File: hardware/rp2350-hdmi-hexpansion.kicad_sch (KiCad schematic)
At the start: 6 parts, among them J1 Hexpansion-Connector

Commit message: hardware: schematic v0.1 with JLCPCB parts, BOMs generated from it
- rp2350-hdmi-hexpansion.kicad_sch: full schematic on one A1 sheet
  (RP2354A, TPS2116 mux + TLV62569 buck, TPS61023 HDMI boost, HDMI Type A
  with TPD4E05U06 ESD and PCA9306 DDC, USB-C sink, microSD, Qwiic, SWD,
  DNP PSRAM and EEPROM). Nets via labels; ERC clean except the intended
  HEXP_DET-to-GND warning; netlist checked pin-for-pin against the design.
  Template edge connector, mounting holes and jumper keep their UUIDs.
- lib/jlc.*: symbols, footprints and .wrl 3D models for all 44 LCSC parts
  (easyeda2kicad), added to the project library tables. STEP models are
  git-ignored.
- bom.csv and hexpansion_bom.xlsx regenerated from the schematic with LCSC
  numbers, JLC Basic/Extended, stock and 10-board prices (107 placements,
  about $5.63/board).
- README/HISTORY: design changes, pin-map changes (GPIO27 RGB, 28 badge
  sense, 29 boost EN), backfeed addendum, firmware follow-ups, and open
  items (LS_A/RUN leak, HS_G/HS_H crossing only confirmed on port 4).
  Corrects the PSRAM part: APS6404L-3SQR-ZR is USON-8, the SOP-8 is -SN.

Co-Authored-By: Claude Opus 5.5 <noreply@anthropic.com>
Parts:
- removed D1: LED, LED_SMD:LED_0805_2012Metric, symbol Device:LED
- removed R1: R, Resistor_SMD:R_0603_1608Metric, symbol Device:R
- added C1, C10, C11, C12, C19, C2, C20, C27, C28, C29, C3, C30, C32, C4, C5, C6, C7, C8, C9: 100nF, jlc:C0402, symbol jlc:CL05B104KO5NNNC
- added C13, C14, C15, C31: 4.7uF, jlc:C0402, symbol jlc:CL05A475MP5NRNC
- added C16, C21, C23, C25: 10uF, jlc:C0603, symbol jlc:CL10A106KP8NNNC
- added C17, C18: 15pF, jlc:C0402, symbol jlc:0402CG150J500NT
- added C22, C24, C26: 22uF, jlc:C0805, symbol jlc:CL21A226MAQNNNE
- added D1: SMF5.0A, jlc:SOD-123FL_L2.7-W1.8-LS3.8-RD, symbol jlc:SMF5.0A_C19077497
- added F1: 200mA PTC, jlc:F0805, symbol jlc:JK-SMD0805-020-30V
- added J1: HDMI-A, jlc:HDMI-SMD_19P-P0.50-H-F, symbol jlc:HDMI-001
- added J2: USB-C, jlc:USB-C-SMD_TYPE-C-16PIN-2MD-073, symbol jlc:TYPE-C16PIN2MD
- added J3: SWD, jlc:CONN-SMD-3P-P1.00_BM03B-SRSS-TB-LF-SN, symbol jlc:BM03B-SRSS-TB
- added J4: Qwiic, jlc:CONN-SMD_4P-P1.00_SM04B-SRSS-TB-LF-SN, symbol jlc:SM04B-SRSS-TB
- added J5: microSD, jlc:TF-SMD_TF-01A, symbol jlc:TF-01A
- added L1: 3.3uH, jlc:IND-SMD_L2.0-W1.6_AOTA-B201610S3R3-101-T, symbol jlc:AOTA-B201610S3R3-101-T
- added L2: 2.2uH, jlc:IND-SMD_L2.5-W2.0_MHCHL2520, symbol jlc:FTC252012S2R2MBCA
- added L3: 1uH, jlc:IND-SMD_L2.5-W2.0_FTC252010S, symbol jlc:FTC252010S1R0MBCA
- added LED1: PWR, jlc:LED-SMD_L1.6-W0.8-R-RD, symbol jlc:KT-0603R
- added LED2: STATUS, jlc:LED-SMD_L1.6-W0.8-R-RD, symbol jlc:KT-0603R
- added LED3: SK6805, jlc:LED-SMD_4P-L2.7-W2.4_SK6805MICRO-J, symbol jlc:SK6805MICRO-J
- added R1, R36, R37, R38, R39: 33R, jlc:R0402, symbol jlc:0402WGF330JTCE
- added R10, R11: 27R, jlc:R0402, symbol jlc:0402WGF270JTCE
- added R12, R16, R17, R18, R34, R35: 100k, jlc:R0402, symbol jlc:0402WGF1003TCE
- added R13, R15: 22k, jlc:R0402, symbol jlc:0402WGF2202TCE
- added R14: 33k, jlc:R0402, symbol jlc:0402WGF3302TCE
- added R19, R29: 200k, jlc:R0402, symbol jlc:0402WGF2003TCE
- added R2, R40, R51, R6: 1k, jlc:R0402, symbol jlc:0402WGF1001TCE
- added R20: 27k, jlc:R0402, symbol jlc:0402WGF2702TCE
- added R21, R22, R23, R24, R25, R26, R27, R28, R4: 0R, jlc:R0402, symbol jlc:0402WGF0000TCE
- added R3, R41, R42, R43, R44, R45, R46, R47, R5, R7: 10k, jlc:R0402, symbol jlc:0402WGF1002TCE
- added R30, R31, R48, R49, R50: 4.7k, jlc:R0402, symbol jlc:0402WGF4701TCE
- added R32, R33: 2k, jlc:R0402, symbol jlc:0402WGF2001TCE
- added R52: 330R, jlc:R0402, symbol jlc:0402WGF3300TCE
- added R8, R9: 5.1k, jlc:R0402, symbol jlc:0402WGF5101TCE
- added SW1: BOOTSEL, jlc:SW-SMD_L3.9-W3.0-P4.45, symbol jlc:TS-1088-AR02016
- added SW2: RESET, jlc:SW-SMD_L3.9-W3.0-P4.45, symbol jlc:TS-1088-AR02016
- added TP1: +3V3, TestPoint:TestPoint_Pad_D1.0mm, symbol Connector:TestPoint
- added TP2: V5_HDMI, TestPoint:TestPoint_Pad_D1.0mm, symbol Connector:TestPoint
- added TP3: GND, TestPoint:TestPoint_Pad_D1.0mm, symbol Connector:TestPoint
- added U1: RP2354A, jlc:QFN-60_L7.0-W7.0-P0.40-TL-EP3.4, symbol jlc:RP2354A
- added U10: ZD24C64A (fallback), jlc:SOP-8_L4.9-W3.9-P1.27-LS6.0-BL, symbol jlc:ZD24C64A-SSGMT
- added U2: TPS2116DRLR, jlc:SOT-583-8_L2.1-W1.6-P0.50-LS1.6-BL, symbol jlc:TPS2116DRLR
- added U3: TLV62569DBVR, jlc:SOT-23-5_L3.0-W1.7-P0.95-LS2.8-BR, symbol jlc:TLV62569DBVR
- added U4: TPS61023DRLR, jlc:SOT-563_L1.6-W1.2-P0.50-LS1.6-BR, symbol jlc:TPS61023DRLR
- added U5: PCA9306DCUR, jlc:SSOP-8_L2.0-W2.3-P0.50-LS3.1-BR, symbol jlc:PCA9306DCUR
- added U6, U7: TPD4E05U06, jlc:USON-10_L2.5-W1.0-P0.50-BL, symbol jlc:TPD4E05U06DQAR_C138714
- added U8: USBLC6-2SC6, jlc:SOT-23-6_L2.9-W1.6-P0.95-LS2.8-BL, symbol jlc:USBLC6-2SC6_C2687116
- added U9: APS6404L-3SQR-SN, jlc:SOIC-8_L4.9-W3.9-P1.27-LS6.0-BL, symbol jlc:APS6404L-3SQR-SN_C5333729
- added Y1: 12MHz, jlc:CRYSTAL-SMD_4P-L3.2-W2.5-BL, symbol jlc:ABM8-272-T3_C20625731
- H1, H2: value MountingHole_Pad -> MountingHole
- J6: renamed from J1; now in the parts list
- JP1: value SolderJumper_2_Bridged -> Qwiic pull-ups
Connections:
- net GND: now also J6.6 (HEXP_DET), C1.2, C10.2, C11.2, C12.2, C13.2, C14.2, C15.2, C16.2, C17.2, C18.2, C19.2, C2.2, C20.2, C21.2, C22.2, C23.2, C24.2, C25.2, C26.2, C27.2, C28.2, C29.2, C3.2, C30.2, C31.2, C32.2, C4.2, C5.2, C6.2, C7.2, C8.2, C9.2, D1.2 (A), J1.11 (TMDSClockShield), J1.17 (DDC/CECGround), J1.2 (TMDSData2Shield), J1.20, J1.21, J1.22, J1.23, J1.5 (TMDSData1Shield), J1.8 (TMDSData0Shield), J2.13 (EH), J2.14 (EH), J2.A1B12 (GND), J2.B1A12 (GND), J3.2, J4.1, J5.10 (GND), J5.11 (GND), J5.12 (GND), J5.13 (GND), J5.6 (VSS), LED1.2 (K), LED2.2 (K), LED3.1 (GND), R13.2, R15.2, R17.2, R18.2, R20.2, R35.2, R8.2, R9.2, SW1.2, SW2.2, TP3.1, U1.47 (VREG_PGND), U1.61 (EP), U10.1 (A0), U10.2 (A1), U10.3 (A2), U10.4 (GND), U10.7 (WP), U2.1 (GND), U3.2 (GND), U4.4 (GND), U5.1 (GND), U6.3 (GND), U6.8 (GND), U7.3 (GND), U7.8 (GND), U8.2 (GND), U9.4 (VSS), Y1.2 (GND), Y1.4 (GND); no longer JP1.2 (B)
- net HS_F: now also R36.1
- net HS_G: now also R38.1
- net HS_H: now also R37.1, R41.2
- net HS_I: now also R39.1
- net LS_A: now reaches J6.2 (LS_A)
- net LS_A: now also R4.1
- net LS_B: now reaches J6.3 (LS_B)
- net LS_B: now also R40.1
- net 3V3 renamed 3V3_BADGE
- net 3V3_BADGE: now also C23.1, C29.1, R16.1, R41.1, U10.8 (VCC), U2.6 (VIN2)
- net HEXP_DET renamed +3V3
- net +3V3: now also C1.1, C14.1, C16.1, C2.1, C20.1, C24.1, C25.1, C3.1, C30.1, C31.1, C32.1, C4.1, C5.1, C6.1, C7.1, C8.1, C9.1, J4.2, J5.4 (VDD), L3.1, LED3.3 (VDD), R1.1, R3.1, R30.1, R31.1, R42.1, R43.1, R44.1, R45.1, R46.1, R47.1, R5.1, R50.1, R7.1, TP1.1, U1.1 (IOVDD), U1.11 (IOVDD), U1.20 (IOVDD), U1.30 (IOVDD), U1.38 (IOVDD), U1.44 (ADC_AVDD), U1.45 (IOVDD), U1.49 (VREG_VIN), U1.53 (USB_OTP_VDD), U1.54 (QSPI_IOVDD), U2.2 (VOUT), U2.7 (VOUT), U4.3 (VIN), U5.2 (VREF1), U9.8 (VDD); no longer J6.6 (HEXP_DET)
- net LS_C: no longer names the net of J6.7 (LS_C)
- net LS_D: no longer names the net of J6.8 (LS_D)
- net LS_E: no longer names the net of J6.9 (LS_E)
- net SCL renamed BADGE_SCL
- net BADGE_SCL: now also U1.37 (GPIO25), U10.6 (SCL)
- net SDA renamed BADGE_SDA
- net BADGE_SDA: now also U1.36 (GPIO24), U10.5 (SDA)
- new net 3V3_USB: C22.1, L2.2, R12.1, R14.1, U2.3 (VIN1), U2.5 (MODE)
- new net BADGE_IRQ: R40.2, U1.40 (GPIO26_ADC0)
- new net BADGE_SENSE: R16.2, R17.1, U1.42 (GPIO28_ADC2)
- new net BOOST_EN: R18.1, U1.43 (GPIO29_ADC3), U4.2 (EN)
- new net BOOST_FB: R19.2, R20.1, U4.1 (FB)
- new net BOOST_SW: L3.2, U4.5 (SW)
- new net BOOTSEL_SW: R6.2, SW1.1
- new net BUCK_FB: R12.2, R13.1, U3.5 (FB)
- new net BUCK_SW: L2.1, U3.3 (SW)
- new net CC1: J2.A5 (CC1), R8.1
- new net CC2: J2.B5 (CC2), R9.1
- new net DDC_EN: C28.1, R29.2, U5.7 (VREF2), U5.8 (EN)
- new net DDC_SCL_3V3: R30.2, U1.7 (GPIO4), U5.3 (SCL1)
- new net DDC_SDA_3V3: R31.2, U1.5 (GPIO3), U5.4 (SDA1)
- new net DVDD: C10.1, C11.1, C12.1, C13.1, L1.2, U1.23 (DVDD), U1.39 (DVDD), U1.50 (VREG_FB), U1.6 (DVDD)
- new net HDMI_CK_N: J1.12 (TMDSClock-), R24.2, U6.5 (D2-), U6.6 (NC)
- new net HDMI_CK_P: J1.10 (TMDSClock+), R23.2, U6.4 (D2+), U6.7 (NC)
- new net HDMI_D0_N: J1.9 (TMDSData0-), R28.2, U7.5 (D2-), U7.6 (NC)
- new net HDMI_D0_P: J1.7 (TMDSData0+), R27.2, U7.4 (D2+), U7.7 (NC)
- new net HDMI_D1_N: J1.6 (TMDSData1-), R26.2, U7.2 (D1-), U7.9 (NC)
- new net HDMI_D1_P: J1.4 (TMDSData1+), R25.2, U7.1 (D1+), U7.10 (NC)
- new net HDMI_D2_N: J1.3 (TMDSData2-), R22.2, U6.2 (D1-), U6.9 (NC)
- new net HDMI_D2_P: J1.1 (TMDSData2+), R21.2, U6.1 (D1+), U6.10 (NC)
- new net HDMI_HPD: J1.19 (HotPlugDetect), R34.1
- new net HDMI_SCL: J1.15 (SCL), R32.2, U5.6 (SCL2)
- new net HDMI_SDA: J1.16 (SDA), R33.2, U5.5 (SDA2)
- new net HPD_SENSE: R34.2, R35.1, U1.4 (GPIO2)
- new net LED1_A: LED1.1 (A), R50.2
- new net LED2_A: LED2.1 (A), R51.2
- new net LED_STATUS: R51.1, U1.3 (GPIO1)
- new net MUX_PR1: R14.2, R15.1, U2.4 (PR1)
- new net PSRAM_CS: R7.2, U1.2 (GPIO0), U9.1 (~{CE})
- new net QSPI_SCLK: U1.56 (QSPI_SCLK), U9.6 (SCLK)
- new net QSPI_SD0: U1.57 (QSPI_SD0), U9.5 (SI/SIO[0])
- new net QSPI_SD1: U1.59 (QSPI_SD1), U9.2 (SO/SIO[1])
- new net QSPI_SD2: U1.58 (QSPI_SD2), U9.3 (SIO[2])
- new net QSPI_SD3: U1.55 (QSPI_SD3), U9.7 (SIO[3])
- new net QSPI_SS: R5.2, R6.1, U1.60 (QSPI_SS)
- new net QWIIC_PU: JP1.2 (B), R48.1, R49.1
- new net QWIIC_SCL: J4.4, R49.2, U1.10 (GPIO7)
- new net QWIIC_SDA: J4.3, R48.2, U1.9 (GPIO6)
- new net RGB_DIN: R52.1, U1.41 (GPIO27_ADC1)
- new net RGB_DIN_R: LED3.2 (DIN), R52.2
- new net RUN: C19.1, R3.2, R4.2, SW2.1, U1.26 (RUN)
- new net SD_CD: J5.9 (CD), R47.2, U1.8 (GPIO5)
- new net SD_CS: J5.2 (CDDAT3(CS)), R43.2, U1.13 (GPIO9)
- new net SD_DAT1: J5.8 (DAT1(RSV)), R46.2
- new net SD_DAT2: J5.1 (DAT2(RSV)), R42.2
- new net SD_MISO: J5.7 (DAT0(D0)), R45.2, U1.12 (GPIO8)
- new net SD_MOSI: J5.3 (CMD(DI)), R44.2, U1.15 (GPIO11)
- new net SD_SCK: J5.5 (CLK(SCLK)), U1.14 (GPIO10)
- new net SPI_CS: R37.2, U1.33 (GPIO21)
- new net SPI_MISO: R39.2, U1.35 (GPIO23)
- new net SPI_MOSI: R36.2, U1.32 (GPIO20)
- new net SPI_SCK: R38.2, U1.34 (GPIO22)
- new net SWCLK: J3.1, U1.24 (SWCLK)
- new net SWDIO: J3.3, U1.25 (SWDIO)
- new net TMDS_CK_N: R24.1, U1.19 (GPIO15)
- new net TMDS_CK_P: R23.1, U1.18 (GPIO14)
- new net TMDS_D0_N: R28.1, U1.31 (GPIO19)
- new net TMDS_D0_P: R27.1, U1.29 (GPIO18)
- new net TMDS_D1_N: R26.1, U1.28 (GPIO17)
- new net TMDS_D1_P: R25.1, U1.27 (GPIO16)
- new net TMDS_D2_N: R22.1, U1.17 (GPIO13)
- new net TMDS_D2_P: R21.1, U1.16 (GPIO12)
- new net USB_CONN_DN: J2.A7 (Dn1), J2.B7 (Dn2), R11.1, U8.3 (I/O2), U8.4 (I/O2)
- new net USB_CONN_DP: J2.A6 (Dp1), J2.B6 (Dp2), R10.1, U8.1 (I/O1), U8.6 (I/O1)
- new net USB_DN: R11.2, U1.51 (USB_DM)
- new net USB_DP: R10.2, U1.52 (USB_DP)
- new net V5_BOOST: C26.1, F1.1, R19.1, U4.6 (VOUT)
- new net V5_HDMI: C27.1, F1.2, J1.18 (+5VPower), R29.1, R32.1, R33.1, TP2.1
- new net VBUS: C21.1, D1.1 (K), J2.A4B9 (VBUS), J2.B4A9 (VBUS), U3.1 (EN), U3.4 (VIN), U8.5 (VBUS)
- new net VREG_AVDD: C15.1, R1.2, U1.46 (VREG_AVDD)
- new net VREG_LX: L1.1, U1.48 (VREG_LX)
- new net XIN: C17.1, U1.21 (XIN), Y1.1
- new net XOUT: R2.1, U1.22 (XOUT)
- new net XOUT_XTAL: C18.1, R2.2, Y1.3
- no-connect marks 0 -> 13
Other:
- note added: "HDMI +5V boost (enabled by GPIO29)"
- note added: "HDMI Type A (DVI over HSTX)"
- note added: "Hexpansion edge connector (badge side)"
- note added: "LEDs, test pads, mounting"
- note added: "MCU - RP2354A (2 MB flash in package)"
- note added: "Notes: - Design rule: this hexpansion never powers the badge (HISTORY.md section 4.5). - Pull-ups on badge-facing lines go to 3V3_BADGE, never +3V3. No pull-ups on BADGE_SDA/SCL (badge has them). - Firmware: tri-state SPI_MISO and BADGE_IRQ until BADGE_SENSE (GPIO28) reads the badge rail live. - Firmware: do not enable internal pull-ups on BADGE_SDA/SCL (GPIO24/25). - OPEN: RUN pull-up (R3) can l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"
- note added: "PSRAM - DNP, hand-solder (QSPI CS1 = GPIO0)"
- note added: "Power mux - never back-powers the badge"
- note added: "Reset, BOOTSEL, SWD"
- note added: "USB-C input (sink only) and 5V -> 3V3 buck"
- note added: "microSD (SPI1) and Qwiic (I2C1)"
- title: (none) -> Hexi-GFX RP2354A HDMI hexpansion
- moved on the sheet: J6

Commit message: hardware: trim schematic - drop DDC, microSD, 0R TMDS and extra passives
- Drop HDMI DDC/EDID (U5 PCA9306 + 6 passives): output is fixed
  640x480@60, so nothing to read. HPD kept on GPIO2.
- Drop microSD (J5, 2 pull-ups, 1 cap): frees the second side flat.
- Drop the eight 0R TMDS insurance resistors; GPIO12-19 drive the ESD
  arrays and socket directly, as on the bench.
- Decoupling cut to the Raspberry Pi minimal design (7 x 100nF on 3V3,
  pins 44/45 and 53/54 share); no BOOTSEL pull-up (internal), no RUN
  debounce cap, no extra HDMI 5V / SD caps.
- Spare GPIOs now 3, 4, 5, 8-11 (no-connect).
- ERC clean except the intended HEXP_DET warning; netlist re-verified
  pin-for-pin (337 pins).
- BOMs regenerated: 78 JLC placements, about $5.01/board (was 107, $5.63).
- README/HISTORY updated with the trims and the microSD decision.

Co-Authored-By: Claude Opus 5.5 <noreply@anthropic.com>
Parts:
- removed C19, C27, C28, C30, C8, C9: 100nF, jlc:C0402, symbol jlc:CL05B104KO5NNNC
- removed C31: 4.7uF, jlc:C0402, symbol jlc:CL05A475MP5NRNC
- removed J5: microSD, jlc:TF-SMD_TF-01A, symbol jlc:TF-01A
- removed R21, R22, R23, R24, R25, R26, R27, R28: 0R, jlc:R0402, symbol jlc:0402WGF0000TCE
- removed R29: 200k, jlc:R0402, symbol jlc:0402WGF2003TCE
- removed R30, R31: 4.7k, jlc:R0402, symbol jlc:0402WGF4701TCE
- removed R32, R33: 2k, jlc:R0402, symbol jlc:0402WGF2001TCE
- removed R42, R43, R44, R45, R46, R47, R5: 10k, jlc:R0402, symbol jlc:0402WGF1002TCE
- removed U5: PCA9306DCUR, jlc:SSOP-8_L2.0-W2.3-P0.50-LS3.1-BR, symbol jlc:PCA9306DCUR
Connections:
- net TMDS_CK_N is gone; now on net HDMI_CK_N: U1.19 (GPIO15)
- net TMDS_CK_P is gone; now on net HDMI_CK_P: U1.18 (GPIO14)
- net TMDS_D0_N is gone; now on net HDMI_D0_N: U1.31 (GPIO19)
- net TMDS_D0_P is gone; now on net HDMI_D0_P: U1.29 (GPIO18)
- net TMDS_D1_N is gone; now on net HDMI_D1_N: U1.28 (GPIO17)
- net TMDS_D1_P is gone; now on net HDMI_D1_P: U1.27 (GPIO16)
- net TMDS_D2_N is gone; now on net HDMI_D2_N: U1.17 (GPIO13)
- net TMDS_D2_P is gone; now on net HDMI_D2_P: U1.16 (GPIO12)
- net DDC_SCL_3V3: no longer names the net of U1.7 (GPIO4)
- net DDC_SDA_3V3: no longer names the net of U1.5 (GPIO3)
- net HDMI_SCL: no longer names the net of J1.15 (SCL)
- net HDMI_SDA: no longer names the net of J1.16 (SDA)
- net SD_CD: no longer names the net of U1.8 (GPIO5)
- net SD_CS: no longer names the net of U1.13 (GPIO9)
- net SD_MISO: no longer names the net of U1.12 (GPIO8)
- net SD_MOSI: no longer names the net of U1.15 (GPIO11)
- net SD_SCK: no longer names the net of U1.14 (GPIO10)
- no-connect marks 13 -> 22
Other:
- note added: "Qwiic (I2C1)"
- note removed: "microSD (SPI1) and Qwiic (I2C1)"
- moved on the sheet: C10, C11, C12, C13, C14, C15, C16, C17, C18, C20, C21, C22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

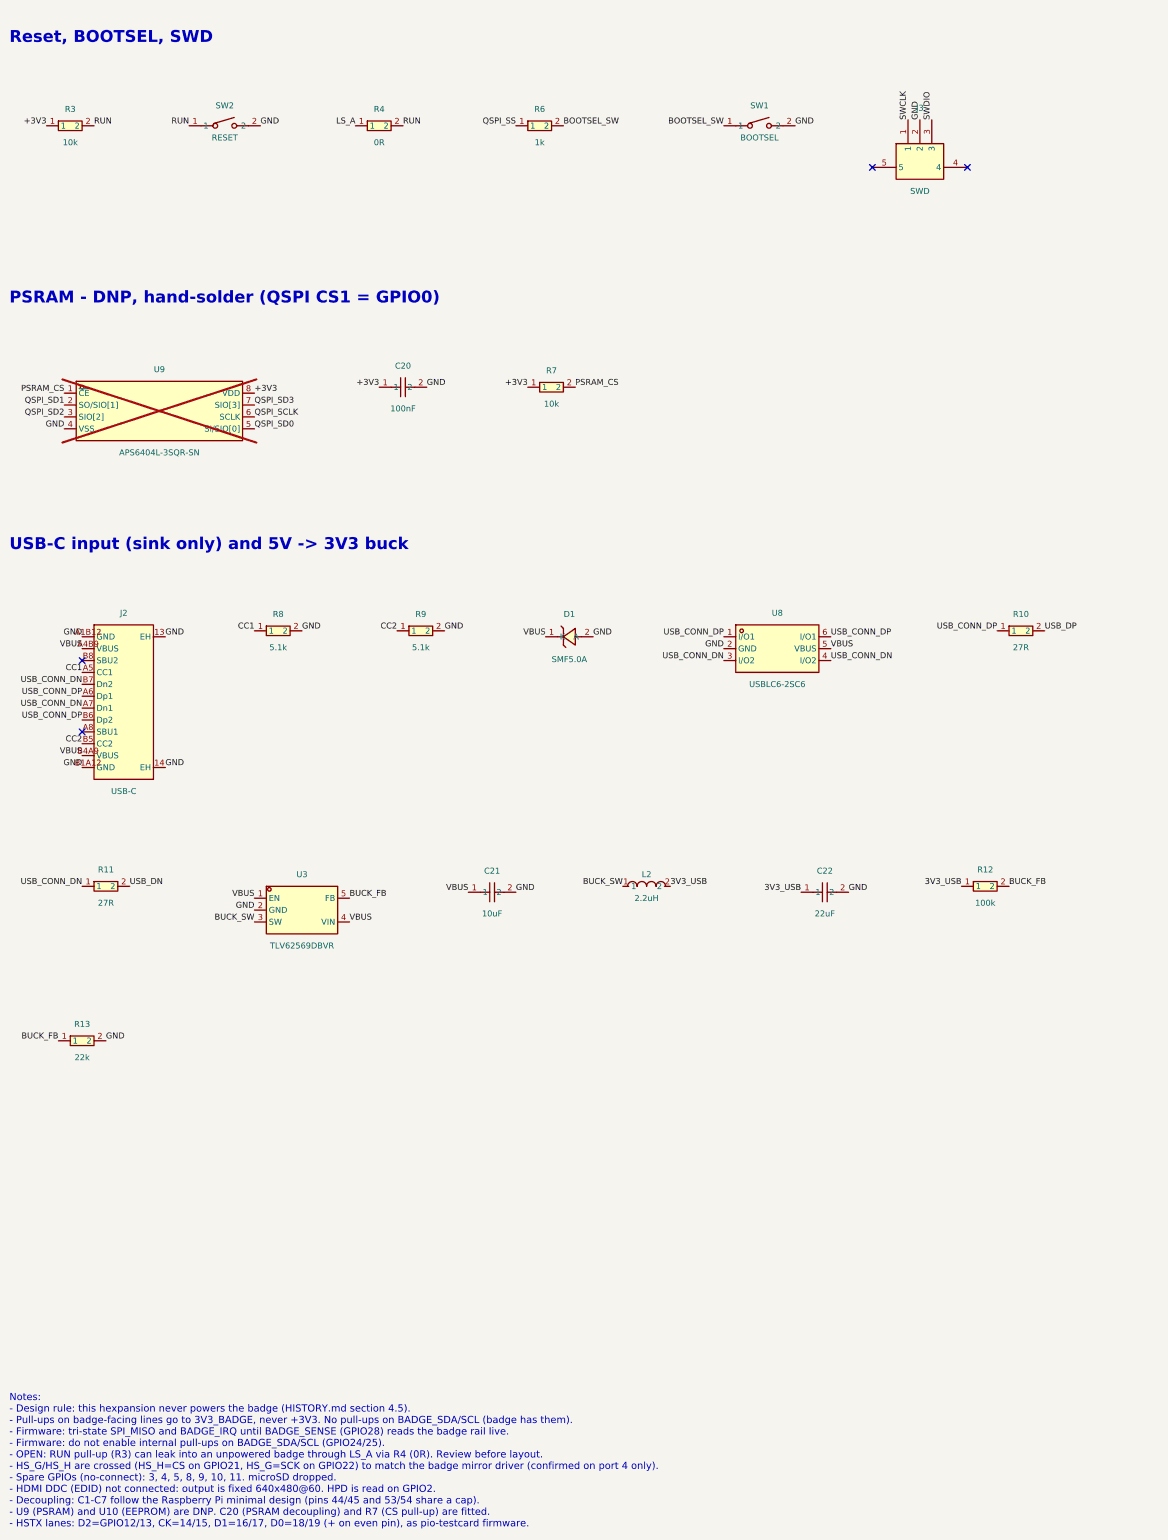
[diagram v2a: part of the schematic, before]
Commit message: hardware: backfeed-proof badge reset via open-drain buffer
LS_A previously reached RUN through a 0R link, so the RUN pull-up could
leak into an unpowered badge. LS_A now drives RUN through U11, an
SN74LVC1G07 open-drain buffer (C7829) powered from 3V3_BADGE, with C33
decoupling and R4 (10k) pulling LS_A up to 3V3_BADGE so it idles at
"not reset". With the badge off, the buffer's Ioff spec (<=10 uA) blocks
the path and the RP2354A keeps running from USB.

- lib/jlc: add SN74LVC1G07DBVR symbol
- ERC clean except intended HEXP_DET warning; netlist re-verified
  (344 pins); no resistor links +3V3 to any badge-facing net
- BOMs regenerated: 80 placements, about $5.11/board
- README/HISTORY: close the LS_A/RUN open item

Co-Authored-By: Claude Opus 5.5 <noreply@anthropic.com>
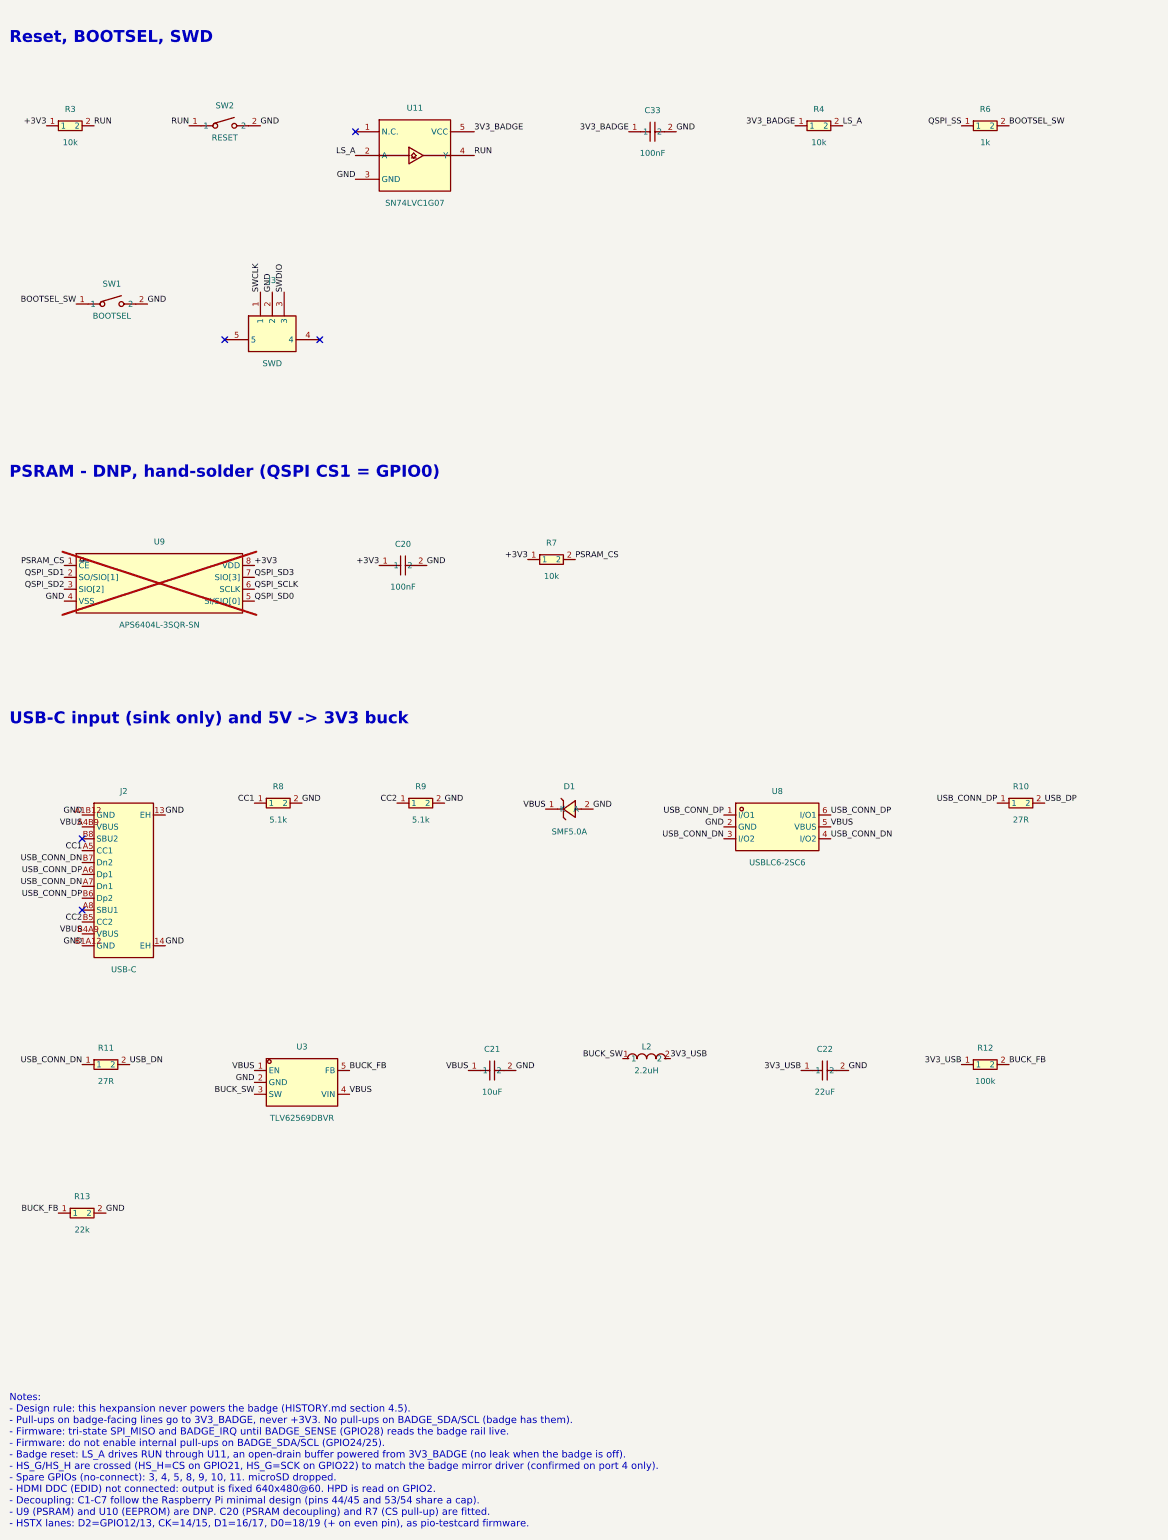
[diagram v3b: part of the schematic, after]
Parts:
- added C33: 100nF, jlc:C0402, symbol jlc:CL05B104KO5NNNC
- added U11: SN74LVC1G07, jlc:SOT-23-5_L3.0-W1.7-P0.95-LS2.8-BR, symbol jlc:SN74LVC1G07DBVR
- R4: value 0R -> 10k; symbol jlc:0402WGF0000TCE -> jlc:0402WGF1002TCE; LCSC Part C17168 -> C25744; MPN 0402WGF0000TCE -> 0402WGF1002TCE
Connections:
- net 3V3_BADGE: now also R4.1, C33.1, U11.5 (VCC)
- net GND: now also C33.2, U11.3 (GND)
- net LS_A: now also R4.2, U11.2 (A); no longer R4.1
- net RUN: now also U11.4 (Y); no longer R4.2
- no-connect marks 22 -> 23
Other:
- note added: "Notes: - Design rule: this hexpansion never powers the badge (HISTORY.md section 4.5). - Pull-ups on badge-facing lines go to 3V3_BADGE, never +3V3. No pull-ups on BADGE_SDA/SCL (badge has them). - Firmware: tri-state SPI_MISO and BADGE_IRQ until BADGE_SENSE (GPIO28) reads the badge rail live. - Firmware: do not enable internal pull-ups on BADGE_SDA/SCL (GPIO24/25). - Badge reset: LS_A drives RUN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"
- note removed: "Notes: - Design rule: this hexpansion never powers the badge (HISTORY.md section 4.5). - Pull-ups on badge-facing lines go to 3V3_BADGE, never +3V3. No pull-ups on BADGE_SDA/SCL (badge has them). - Firmware: tri-state SPI_MISO and BADGE_IRQ until BADGE_SENSE (GPIO28) reads the badge rail live. - Firmware: do not enable internal pull-ups on BADGE_SDA/SCL (GPIO24/25). - OPEN: RUN pull-up (R3) can l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"
- moved on the sheet: C20, C21, C22, D1, J2, J3, L2, R10, R11, R12, R13, R4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
